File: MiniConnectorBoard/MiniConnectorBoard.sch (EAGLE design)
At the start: 4 parts

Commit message: MiniConnectorBoard - first cut
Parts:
- added JP3: NONE, MiniConnectorBoard:PINHD-1X20
- JP2: device HeaderConnectorBoard:PINHD-2X20 -> MiniConnectorBoard:PINHD-1X20
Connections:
- net 10/MOSI: now also JP3.10; no longer JP2.20
- net 11/CLK: now also JP3.12; no longer JP2.24
- net 12: now also JP2.16; no longer JP2.31
- net 13: now also JP3.17; no longer JP2.34
- net 14/TX: now also JP2.4; no longer JP2.7
- net 15/RX: now also JP2.5; no longer JP2.9
- net 16: now also JP2.18; no longer JP2.35
- net 17/RTS: now also JP3.6; no longer JP2.12
- net 18: now also JP2.6; no longer JP2.11
- net 19: now also JP3.18; no longer JP2.36
- net 2/SDA: now also JP3.2; no longer JP2.4
- net 20: now also JP2.19; no longer JP2.37
- net 21: now also JP2.20; no longer JP2.39
- net 22: now also JP3.8; no longer JP2.16
- net 23: now also JP2.8; no longer JP2.15
- net 24: now also JP2.9; no longer JP2.17
- net 25: now also JP2.11; no longer JP2.21
- net 26: now also JP3.19; no longer JP2.38
- net 27: now also JP3.7; no longer JP2.14
- net 3.3V_1: now also JP3.1; no longer JP2.2
- net 3.3V_2: now also JP3.9; no longer JP2.18
- net 3/SCL: now also JP3.3; no longer JP2.6
- net 4: now also JP3.4; no longer JP2.8
- net 5: now also JP3.15; no longer JP2.30
- net 5V_1: now also JP2.2; no longer JP2.3
- net 6: now also JP3.16; no longer JP2.32
- net 7/CE1: now also JP2.13; no longer JP2.25
- net 8/CE0: now also JP2.12; no longer JP2.23
- net 9/MISO: now also JP3.11; no longer JP2.22
- net GND: now also JP3.5; no longer JP2.10
- net GND2: now also JP3.13; no longer JP2.26
- net GND3: now also JP2.10; no longer JP2.19
- net GND4: now also JP2.7; no longer JP2.13
- net GND5: now also JP2.3; no longer JP2.5
- net GND6: now also JP3.20; no longer JP2.40, R1.1
- net GND7: now also JP2.17, R1.1; no longer JP2.33
- net GND8: now also JP2.15; no longer JP2.29
- net ID1: now also JP3.14; no longer JP2.28
- net ID2: now also JP2.14; no longer JP2.27
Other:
- moved on the sheet: LED1, R1

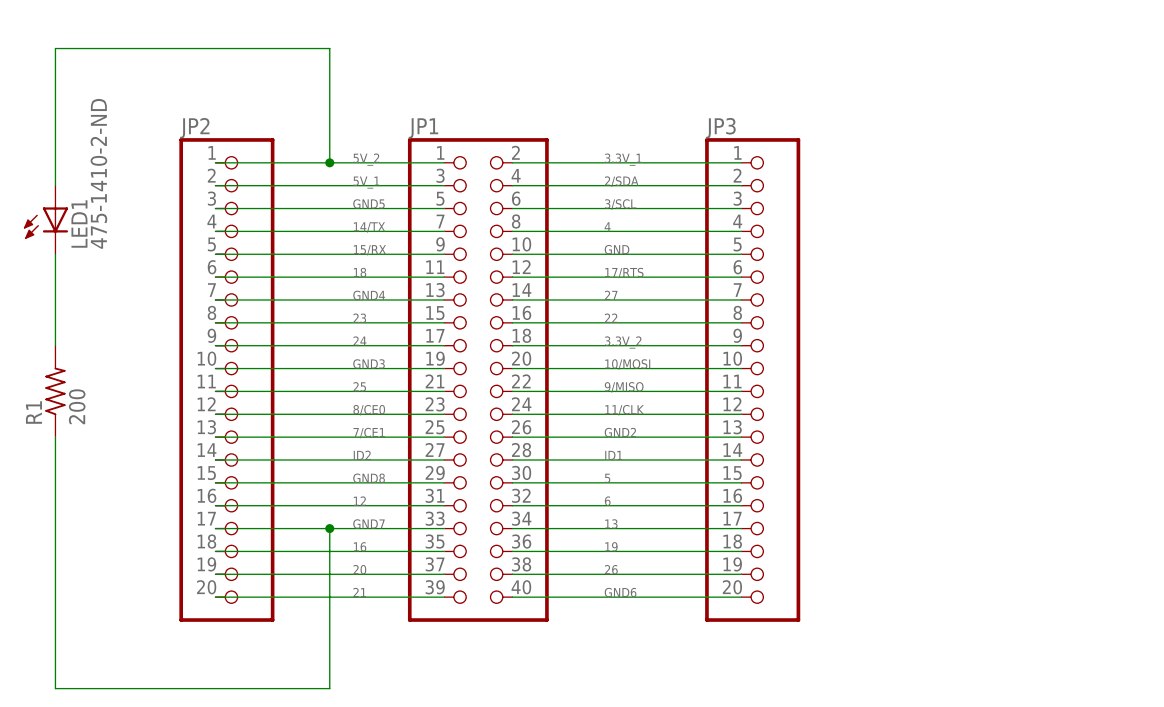
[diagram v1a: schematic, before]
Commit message: MiniConnectorBoard - removed power, added logo, Rev-01b
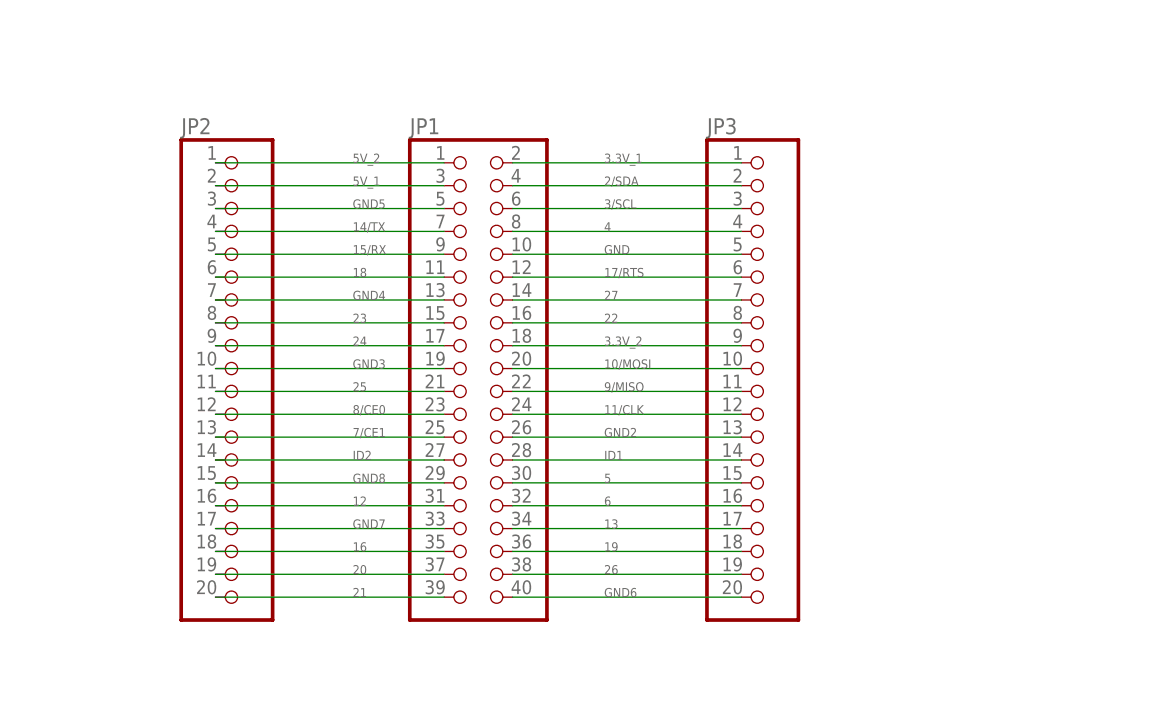
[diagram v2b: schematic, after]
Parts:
- removed LED1: 475-1410-2-ND, led:LEDCHIPLED_0805
- removed R1: 200, resistor:R-US_R0805
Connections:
- removed net N$1: LED1.C, R1.2
- net 5V_2: no longer LED1.A
- net GND7: no longer R1.1
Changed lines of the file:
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@@
 <part name="JP2" library="MiniConnectorBoard" deviceset="PINHD-1X20" device="" value="NONE"/>
 <part name="JP3" library="MiniConnectorBoard" deviceset="PINHD-1X20" device="" value="NONE"/>
-<part name="LED1" library="led" deviceset="LED" device="CHIPLED_0805" value="475-1410-2-ND"/>
-<part name="R1" library="resistor" deviceset="R-US_" device="R0805" value="200"/>
 </parts>
 <sheets>
@@
 <attribute name="NAME" x="62.23" y="107.315" size="1.778" layer="95"/>
 </instance>
-<instance part="LED1" gate="G$1" x="-10.16" y="99.06"/>
-<instance part="R1" gate="G$1" x="-10.16" y="78.74" rot="R90"/>
 </instances>
 <busses>
@@
 <pinref part="JP1" gate="A" pin="1"/>
 <pinref part="JP2" gate="G$1" pin="1"/>
-<wire x1="33.02" y1="104.14" x2="20.32" y2="104.14" width="0.1524" layer="91"/>
-<pinref part="LED1" gate="G$1" pin="A"/>
-<wire x1="20.32" y1="104.14" x2="7.62" y2="104.14" width="0.1524" layer="91"/>
-<wire x1="-10.16" y1="101.6" x2="-10.16" y2="116.84" width="0.1524" layer="91"/>
-<wire x1="-10.16" y1="116.84" x2="20.32" y2="116.84" width="0.1524" layer="91"/>
-<wire x1="20.32" y1="104.14" x2="20.32" y2="116.84" width="0.1524" layer="91"/>
-<junction x="20.32" y="104.14"/>
+<wire x1="33.02" y1="104.14" x2="7.62" y2="104.14" width="0.1524" layer="91"/>
 </segment>
 </net>
@@
 </segment>
 </net>
-<net name="N$1" class="0">
-<segment>
-<pinref part="LED1" gate="G$1" pin="C"/>
-<pinref part="R1" gate="G$1" pin="2"/>
-<wire x1="-10.16" y1="93.98" x2="-10.16" y2="83.82" width="0.1524" layer="91"/>
-</segment>
-</net>
 <net name="GND6" class="0">
 <segment>
@@
 <net name="GND7" class="0">
 <segment>
-<pinref part="R1" gate="G$1" pin="1"/>
-<wire x1="-10.16" y1="73.66" x2="-10.16" y2="45.72" width="0.1524" layer="91"/>
 <pinref part="JP1" gate="A" pin="33"/>
 <label x="22.86" y="63.5" size="1.016" layer="95"/>
 <pinref part="JP2" gate="G$1" pin="17"/>
-<wire x1="33.02" y1="63.5" x2="20.32" y2="63.5" width="0.1524" layer="91"/>
-<wire x1="20.32" y1="63.5" x2="7.62" y2="63.5" width="0.1524" layer="91"/>
-<wire x1="-10.16" y1="45.72" x2="20.32" y2="45.72" width="0.1524" layer="91"/>
-<wire x1="20.32" y1="45.72" x2="20.32" y2="63.5" width="0.1524" layer="91"/>
-<junction x="20.32" y="63.5"/>
-</segment>
-</net>
+<wire x1="33.02" y1="63.5" x2="7.62" y2="63.5" width="0.1524" layer="91"/>
+</segment>
+</net>
